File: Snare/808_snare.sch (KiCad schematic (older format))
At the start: 68 parts

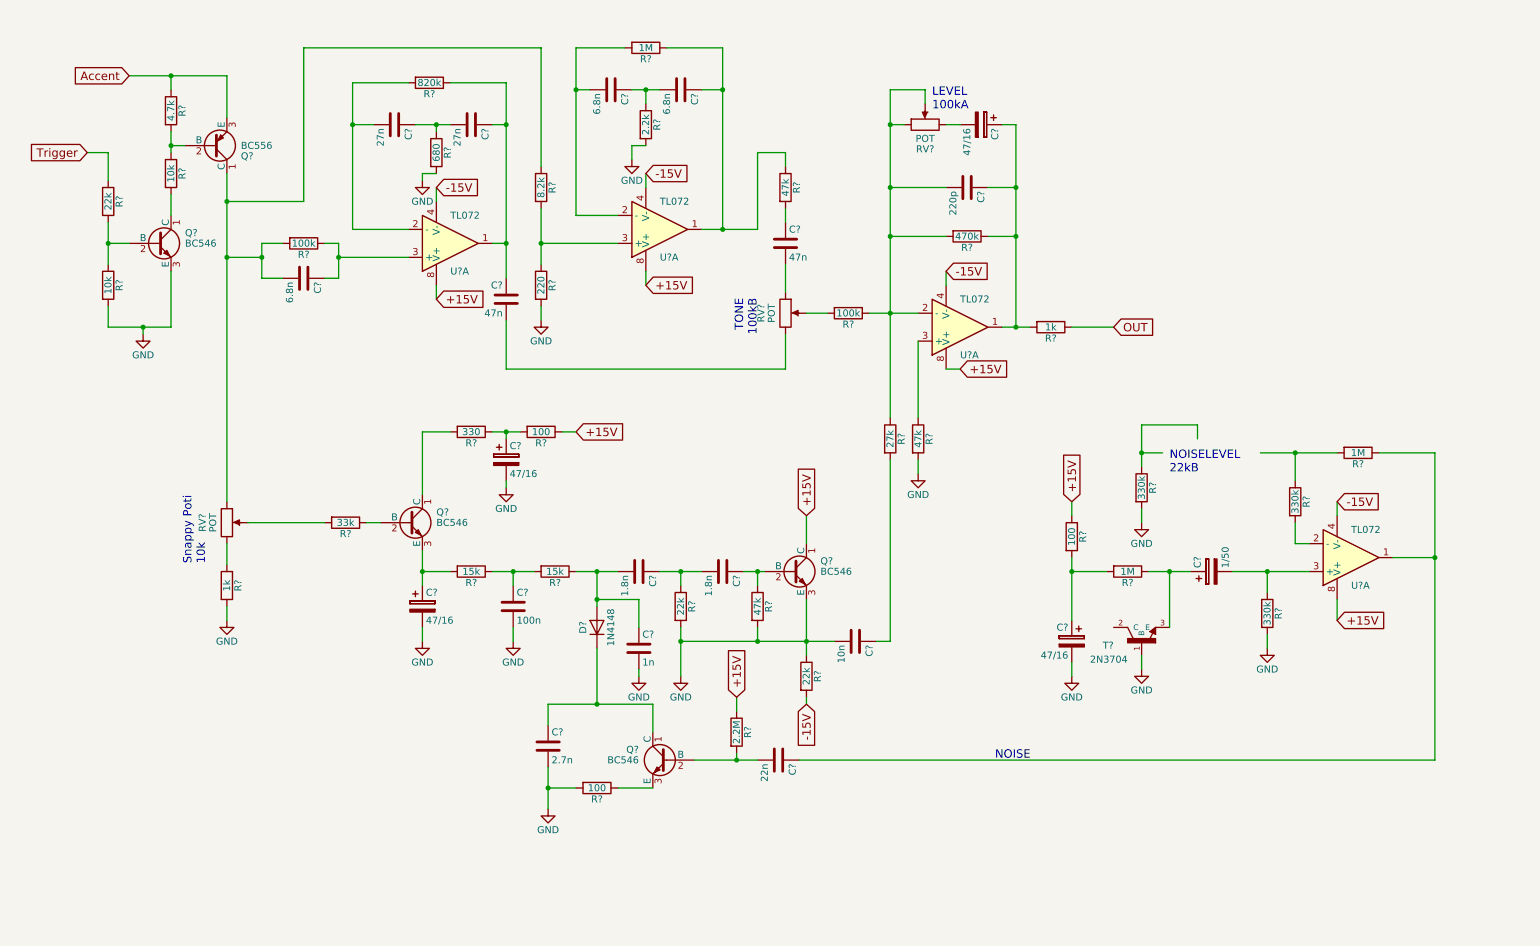
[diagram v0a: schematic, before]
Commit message: added pwr flags to snare
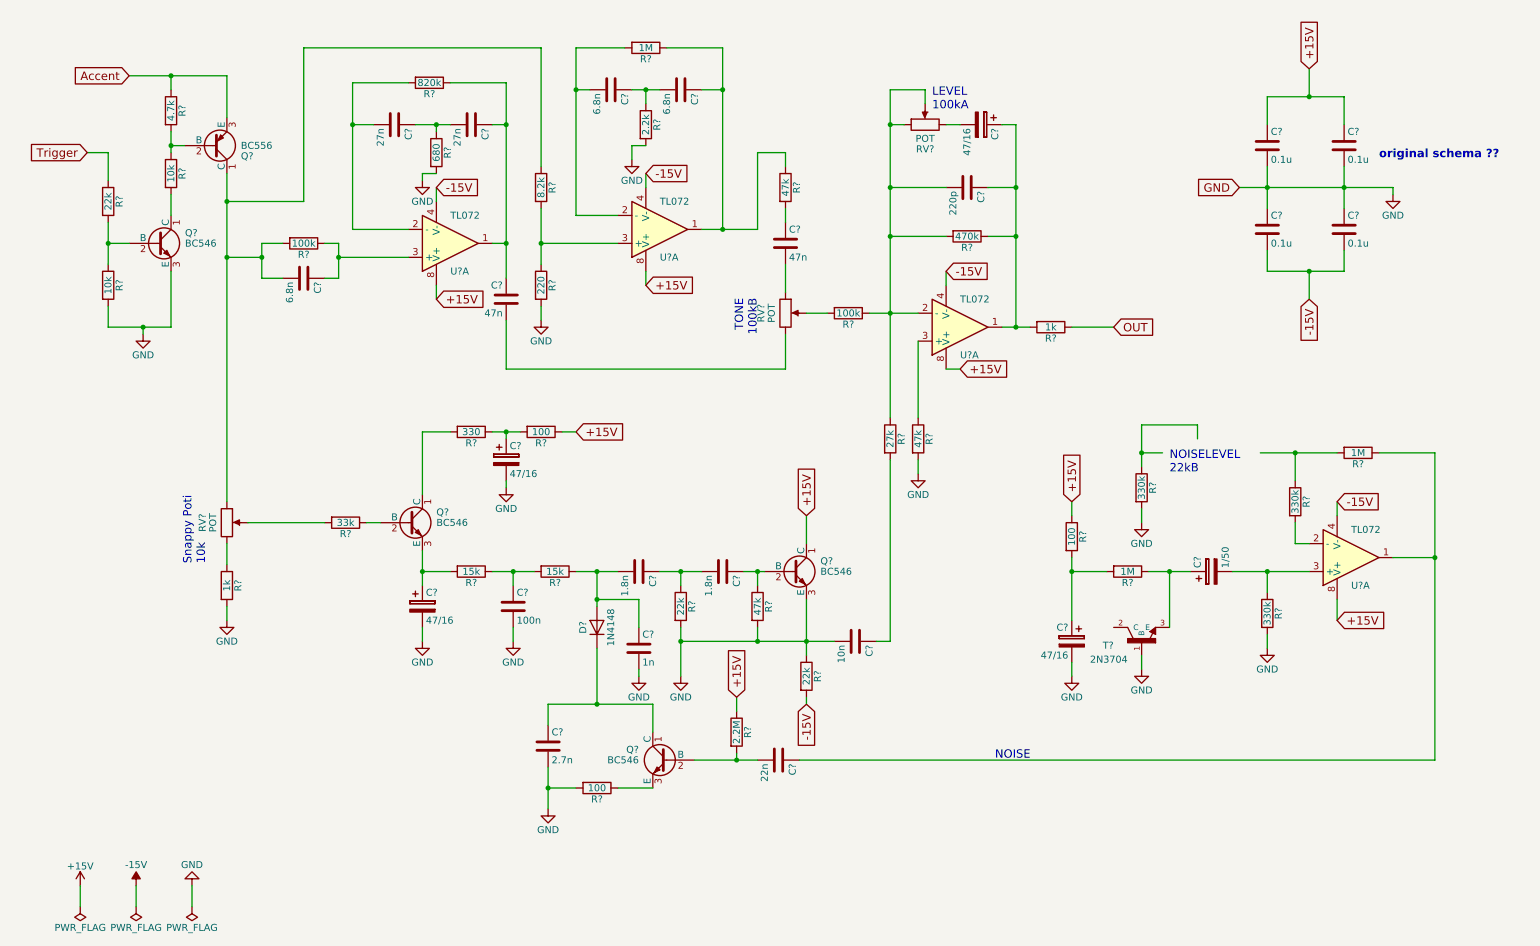
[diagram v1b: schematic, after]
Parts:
- added C? (x4): 0.1u, symbol C
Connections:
- net +15V: now also C?.1, C?.1
- net -15V: now also C?.2, C?.2
- net GND: now also C?.1, C?.1, C?.2, C?.2
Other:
- note added: "original schema ??"
